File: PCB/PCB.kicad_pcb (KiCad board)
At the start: 2 copper layers, 82 x 60 mm, 118 parts, among them J1 Conn_01x02_Pin, J3 Conn_02x16_Odd_Even, J4 USB_C_Receptacle_PowerOnly_6P, SW1 SW_Nidec_CAS-120A1, U1 DRV8833PWPR, U10 TPS63020, U11 TPS63020, U12 TS5A3159ADBVR, U13 CH224K, U2 INA219AxDCN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

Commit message: Fix PCB layout
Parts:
- J1: footprint Connector_JST:JST_JWPF_B02B-JWPF-SK-R_1x02_P2.00mm_Vertical -> Connector_JST:JST_PH_S2B-PH-K_1x02_P2.00mm_Horizontal
- moved U10 233.6 mm to (176.1, 15.4), turned to 180 degrees
- moved R31 172.2 mm to (45.6, 102.0), turned to 90 degrees
- moved TP33 167.5 mm to (47.8, 93.0), turned to 90 degrees
- moved D5 166.7 mm to (55.0, 102.0)
- moved R10 164.0 mm to (52.8, 97.5)
- moved D2 163.2 mm to (57.1, 121.1), turned to -90 degrees
- moved R32 160.3 mm to (56.6, 112.0)
- moved R27 159.5 mm to (40.5, 113.1), turned to -90 degrees
- moved R24 156.3 mm to (43.5, 112.9), turned to -90 degrees
- moved C4 153.8 mm to (33.0, 112.6), turned to -90 degrees
- moved C5 150.3 mm to (36.7, 108.8)
- moved TP24 150.0 mm to (61.6, 101.5)
- moved R20 144.3 mm to (53.0, 104.5), turned to 180 degrees
- moved U3 143.2 mm to (63.6, 98.5)
- moved R19 141.4 mm to (54.1, 121.1), turned to 90 degrees
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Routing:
- net GND: track 459.7 -> 0.00 mm, vias 4 -> 0
- net Load_Supply: track 188.3 -> 0.00 mm, vias 7 -> 0
- net /5V_Out: track 158.0 -> 0.00 mm, vias 5 -> 0
- net High_Voltage_(9V): track 147.1 -> 0.00 mm, vias 7 -> 0
- net /3V3_Out: track 146.9 -> 0.00 mm, vias 5 -> 0
- net EXT_LOAD2_OUT: track 140.0 -> 0.00 mm, vias 2 -> 0
- net Net-(U10-PG): track 131.8 -> 0.00 mm, vias 2 -> 0
- net EXT_LOAD1_OUT: track 131.3 -> 0.00 mm, vias 5 -> 0
- net Net-(JP19-B): track 127.4 -> 0.00 mm, vias 7 -> 0
- net Battery: track 122.5 -> 0.00 mm, vias 4 -> 0
- net MOTOR4_A_OUT: track 111.8 -> 0.00 mm, vias 8 -> 0
- net Net-(JP18-A): track 108.3 -> 0.00 mm, vias 4 -> 0
- net Net-(JP17-B): track 104.0 -> 0.00 mm, vias 5 -> 0
- net Net-(U13-VBUS): track 102.4 -> 0.00 mm, vias 4 -> 0
- net /VBUS: track 101.3 -> 0.00 mm, vias 2 -> 0
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
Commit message: Dummy Commit
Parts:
- added REF**: MountingHole_2.1mm, MountingHole:MountingHole_2.1mm, F.Cu at (53.5, 128.5)
- moved JP16 51.2 mm to (139.2, 135.0)
- moved C2 51.2 mm to (153.0, 139.0)
- moved C3 51.2 mm to (153.0, 141.0)
- moved D1 51.2 mm to (148.4, 145.0)
- moved JP12 51.2 mm to (139.0, 139.0)
- moved JP20 51.2 mm to (138.7, 142.5)
- moved JP25 51.2 mm to (138.7, 146.5)
- moved R14 51.2 mm to (144.1, 145.0)
- moved R23 51.2 mm to (135.0, 137.1)
- moved TP6 51.2 mm to (152.0, 137.0)
- moved TP7 51.2 mm to (154.5, 137.0)
- moved TP8 51.2 mm to (153.0, 148.0)
- moved TP9 51.2 mm to (149.0, 148.5)
- moved U1 51.2 mm to (146.0, 140.0)
- moved C16 51.2 mm to (152.1, 145.0)
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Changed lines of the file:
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@@
 	(footprint "Resistor_SMD:R_0603_1608Metric_Pad0.98x0.95mm_HandSolder"
 		(layer "F.Cu")
-		(at 99.6876 119.4751 180)
+		(at 144.0875 145 180)
 		(descr "Resistor SMD 0603 (1608 Metric), square (rectangular) end terminal, IPC_7351 nominal with elongated pad for handsoldering. (Body size source: IPC-SM-782 page 72, https://www.pcb-3d.com/wordpress/wp-content/uploads/ipc-sm-782a_amendment_1_and_2.pdf), generated with kicad-footprint-generator")
 		(tags "resistor handsolder")
@@
 	(footprint "Jumper:SolderJumper-2_P1.3mm_Open_Pad1.0x1.5mm"
 		(layer "F.Cu")
-		(at 94.35 121 180)
+		(at 138.7499 146.5249 180)
 		(descr "SMD Solder Jumper, 1x1.5mm Pads, 0.3mm gap, open")
 		(tags "solder jumper open")
@@
 	(footprint "TestPoint:TestPoint_Pad_D1.0mm"
 		(layer "F.Cu")
-		(at 107.6001 111.4751)
+		(at 152 137)
 		(descr "SMD pad as test Point, diameter 1.0mm")
 		(tags "test point SMD pad")
@@
 	(footprint "TestPoint:TestPoint_Pad_D1.0mm"
 		(layer "F.Cu")
-		(at 104.6001 122.9751)
+		(at 149 148.5)
 		(descr "SMD pad as test Point, diameter 1.0mm")
 		(tags "test point SMD pad")
@@
 	(footprint "Jumper:SolderJumper-2_P1.3mm_Open_Pad1.0x1.5mm"
 		(layer "F.Cu")
-		(at 94.8 109.5 180)
+		(at 139.1999 135.0249 180)
 		(descr "SMD Solder Jumper, 1x1.5mm Pads, 0.3mm gap, open")
 		(tags "solder jumper open")
@@
 	(footprint "Capacitor_SMD:C_0603_1608Metric_Pad1.08x0.95mm_HandSolder"
 		(layer "F.Cu")
-		(at 107.7376 119.4751 180)
+		(at 152.1375 145 180)
 		(descr "Capacitor SMD 0603 (1608 Metric), square (rectangular) end terminal, IPC_7351 nominal with elongated pad for handsoldering. (Body size source: IPC-SM-782 page 76, https://www.pcb-3d.com/wordpress/wp-content/uploads/ipc-sm-782a_amendment_1_and_2.pdf), generated with kicad-footprint-generator")
 		(tags "capacitor handsolder")
@@
 	(footprint "Resistor_SMD:R_0603_1608Metric_Pad0.98x0.95mm_HandSolder"
 		(layer "F.Cu")
-		(at 90.7 118.9125 90)
+		(at 135.0999 144.4374 90)
 		(descr "Resistor SMD 0603 (1608 Metric), square (rectangular) end terminal, IPC_7351 nominal with elongated pad for handsoldering. (Body size source: IPC-SM-782 page 72, https://www.pcb-3d.com/wordpress/wp-content/uploads/ipc-sm-782a_amendment_1_and_2.pdf), generated with kicad-footprint-generator")
 		(tags "resistor handsolder")
@@
 	(footprint "Capacitor_SMD:C_0603_1608Metric_Pad1.08x0.95mm_HandSolder"
 		(layer "F.Cu")
-		(at 108.6001 113.4751 180)
+		(at 153 139 180)
 		(descr "Capacitor SMD 0603 (1608 Metric), square (rectangular) end terminal, IPC_7351 nominal with elongated pad for handsoldering. (Body size source: IPC-SM-782 page 76, https://www.pcb-3d.com/wordpress/wp-content/uploads/ipc-sm-782a_amendment_1_and_2.pdf), generated with kicad-footprint-generator")
 		(tags "capacitor handsolder")
@@
 	(footprint "LED_SMD:LED_0603_1608Metric_Pad1.05x0.95mm_HandSolder"
 		(layer "F.Cu")
-		(at 103.9751 119.4751 180)
+		(at 148.375 145 180)
 		(descr "LED SMD 0603 (1608 Metric), square (rectangular) end terminal, IPC_7351 nominal, (Body size source: http://www.tortai-tech.com/upload/download/2011102023233369053.pdf), generated with kicad-footprint-generator")
 		(tags "LED handsolder")
@@
 	(footprint "Mix:IC_DRV8833PWPR"
 		(layer "F.Cu")
-		(at 101.6001 114.4751)
+		(at 146 140)
 		(property "Reference" "U1"
 			(at -0.375038 -3.432776 0)
@@
 			(polygon
 				(pts
-					(xy 100.37 115.63) (xy 102.8302 115.63) (xy 102.8302 113.3202) (xy 100.37 113.3202)
+					(xy 144.7699 141.1549) (xy 147.2301 141.1549) (xy 147.2301 138.8451) (xy 144.7699 138.8451)
 				)
 			)
@@
 			(polygon
 				(pts
-					(xy 100.37 115.63) (xy 102.8302 115.63) (xy 102.8302 113.3202) (xy 100.37 113.3202)
+					(xy 144.7699 141.1549) (xy 147.2301 141.1549) (xy 147.2301 138.8451) (xy 144.7699 138.8451)
 				)
 			)
@@
 		)
 	)
+	(footprint "MountingHole:MountingHole_2.1mm"
+		(layer "F.Cu")
+		(at 53.5 128.5)
+		(descr "Mounting Hole 2.1mm, no annular")
+		(tags "mounting hole 2.1mm no annular")
+		(property "Reference" "REF**"
+			(at 0 -3.2 0)
+			(layer "F.SilkS")
+			(effects
+				(font
+					(size 1 1)
+					(thickness 0.15)
+				)
+			)
+		)
+		(property "Value" "MountingHole_2.1mm"
+			(at 0 3.2 0)
+			(layer "F.Fab")
+			(effects
+				(font
+					(size 1 1)
+					(thickness 0.15)
+				)
+			)
+		)
+		(property "Datasheet" ""
+			(at 0 0 0)
+			(unlocked yes)
+			(layer "F.Fab")
+			(hide yes)
+			(effects
+				(font
+					(size 1.27 1.27)
+					(thickness 0.15)
+				)
+			)
+		)
+		(property "Description" ""
+			(at 0 0 0)
+			(unlocked yes)
+			(layer "F.Fab")
+			(hide yes)
+			(effects
+				(font
+					(size 1.27 1.27)
+					(thickness 0.15)
+				)
+			)
+		)
+		(attr exclude_from_pos_files exclude_from_bom)
+		(fp_circle
+			(center 0 0)
+			(end 2.1 0)
+			(stroke
+				(width 0.15)
+				(type solid)
+			)
+			(fill no)
+			(layer "Cmts.User")
+		)
+		(fp_circle
+			(center 0 0)
+			(end 2.35 0)
+			(stroke
+				(width 0.05)
+				(type solid)
+			)
+			(fill no)
+			(layer "F.CrtYd")
+		)
+		(fp_text user "${REFERENCE}"
+			(at 0 0 0)
+			(layer "F.Fab")
+			(effects
+				(font
+					(size 1 1)
+					(thickness 0.15)
+				)
+			)
+		)
+		(pad "" np_thru_hole circle
+			(at 0 0)
+			(size 2.1 2.1)
+			(drill 2.1)
+			(layers "*.Cu" "*.Mask")
+		)
+		(embedded_fonts no)
+	)
 	(footprint "Jumper:SolderJumper-3_P1.3mm_Open_Pad1.0x1.5mm"
 		(layer "F.Cu")
@@
 	(footprint "Capacitor_SMD:C_0603_1608Metric_Pad1.08x0.95mm_HandSolder"
 		(layer "F.Cu")
-		(at 108.6001 115.4751)
+		(at 153 141)
 		(descr "Capacitor SMD 0603 (1608 Metric), square (rectangular) end terminal, IPC_7351 nominal with elongated pad for handsoldering. (Body size source: IPC-SM-782 page 76, https://www.pcb-3d.com/wordpress/wp-content/uploads/ipc-sm-782a_amendment_1_and_2.pdf), generated with kicad-footprint-generator")
 		(tags "capacitor handsolder")
@@
 	(footprint "Jumper:SolderJumper-2_P1.3mm_Open_Pad1.0x1.5mm"
 		(layer "F.Cu")
-		(at 94.35 117 180)
+		(at 138.7499 142.5249 180)
 		(descr "SMD Solder Jumper, 1x1.5mm Pads, 0.3mm gap, open")
 		(tags "solder jumper open")
@@
 	(footprint "TestPoint:TestPoint_Pad_D1.0mm"
 		(layer "F.Cu")
-		(at 110.1001 111.4751)
+		(at 154.5 137)
 		(descr "SMD pad as test Point, diameter 1.0mm")
 		(tags "test point SMD pad")
@@
 	(footprint "Jumper:SolderJumper-2_P1.3mm_Open_Pad1.0x1.5mm"
 		(layer "F.Cu")
-		(at 94.65 113.5 180)
+		(at 139.0499 139.0249 180)
 		(descr "SMD Solder Jumper, 1x1.5mm Pads, 0.3mm gap, open")
 		(tags "solder jumper open")
@@
 	(footprint "Resistor_SMD:R_0603_1608Metric_Pad0.98x0.95mm_HandSolder"
 		(layer "F.Cu")
-		(at 90.65 111.5875 90)
+		(at 135.0499 137.1124 90)
 		(descr "Resistor SMD 0603 (1608 Metric), square (rectangular) end terminal, IPC_7351 nominal with elongated pad for handsoldering. (Body size source: IPC-SM-782 page 72, https://www.pcb-3d.com/wordpress/wp-content/uploads/ipc-sm-782a_amendment_1_and_2.pdf), generated with kicad-footprint-generator")
 		(tags "resistor handsolder")
@@
 	(footprint "TestPoint:TestPoint_Pad_D1.0mm"
 		(layer "F.Cu")
-		(at 108.6001 122.4751)
+		(at 153 148)
 		(descr "SMD pad as test Point, diameter 1.0mm")
 		(tags "test point SMD pad")

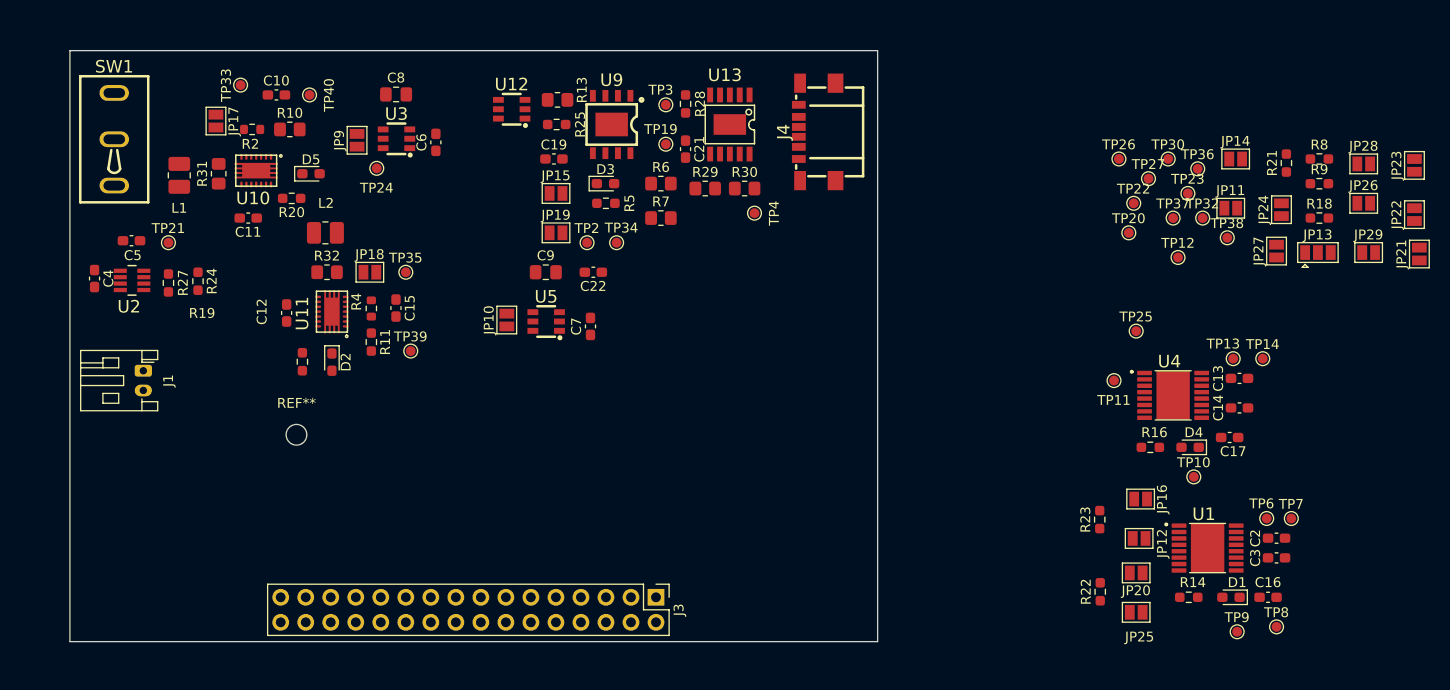
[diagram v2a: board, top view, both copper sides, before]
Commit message: Placing All components onto the silkscreen
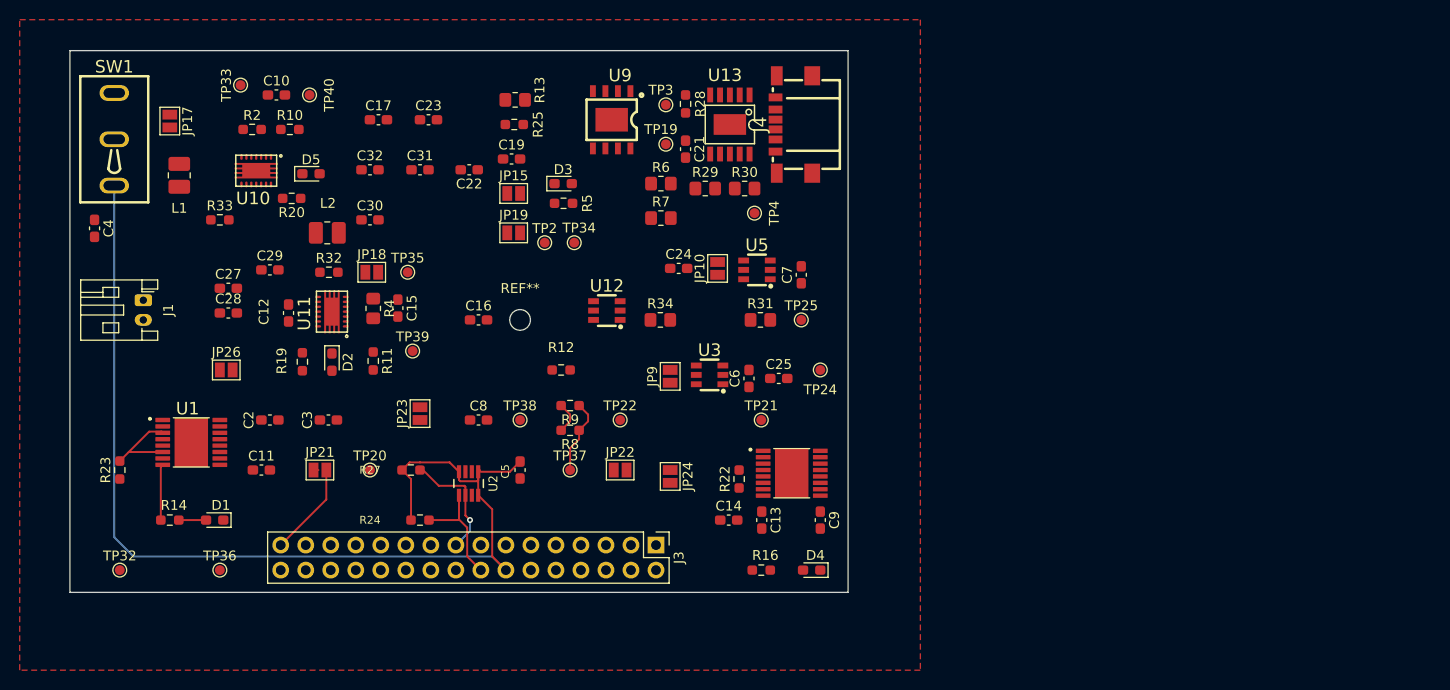
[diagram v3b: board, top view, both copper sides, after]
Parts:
- removed JP11, JP12, JP14, JP16, JP20, JP25, JP27, JP28, JP29: Jumper_2_Small_Open, Jumper:SolderJumper-2_P1.3mm_Open_Pad1.0x1.5mm
- removed JP13: Jumper_3_Open, Jumper:SolderJumper-3_P1.3mm_Open_Pad1.0x1.5mm
- removed R18, R21: 0.22, Resistor_SMD:R_0603_1608Metric_Pad0.98x0.95mm_HandSolder
- removed TP10, TP11, TP12, TP13, TP14, TP23, TP26, TP27, TP30, TP6, TP7, TP8, TP9: TestPoint, TestPoint:TestPoint_Pad_D1.0mm
- added C23: 10u, Capacitor_SMD:C_0603_1608Metric_Pad1.08x0.95mm_HandSolder, F.Cu at (66.9, 96.5)
- added C24: 10u, Capacitor_SMD:C_0603_1608Metric_Pad1.08x0.95mm_HandSolder, F.Cu at (92.3, 111.6)
- added C25: 10u, Capacitor_SMD:C_0603_1608Metric_Pad1.08x0.95mm_HandSolder, F.Cu at (102.5, 122.8)
- added C27: 22u, Capacitor_SMD:C_0603_1608Metric_Pad1.08x0.95mm_HandSolder, F.Cu at (46.6, 113.6)
- added C28: 22u, Capacitor_SMD:C_0603_1608Metric_Pad1.08x0.95mm_HandSolder, F.Cu at (46.6, 116.1)
- added C29: 22u, Capacitor_SMD:C_0603_1608Metric_Pad1.08x0.95mm_HandSolder, F.Cu at (50.8, 111.8)
- added C30: 22u, Capacitor_SMD:C_0603_1608Metric_Pad1.08x0.95mm_HandSolder, F.Cu at (61.0, 106.7)
- added C31: 22u, Capacitor_SMD:C_0603_1608Metric_Pad1.08x0.95mm_HandSolder, F.Cu at (66.0, 101.6)
- added C32: 22u, Capacitor_SMD:C_0603_1608Metric_Pad1.08x0.95mm_HandSolder, F.Cu at (61.0, 101.6)
- added R12: 0.22, Resistor_SMD:R_0603_1608Metric_Pad0.98x0.95mm_HandSolder, F.Cu at (80.4, 121.9)
- added R33: 510k, Resistor_SMD:R_0603_1608Metric_Pad0.98x0.95mm_HandSolder, F.Cu at (45.7, 106.7)
- added R34: 10k, Resistor_SMD:R_0805_2012Metric_Pad1.20x1.40mm_HandSolder, F.Cu at (90.4, 116.8)
- C11: value 10u -> 100n
- C13, C16, C17: value 2.2u -> 10u
- C14: value 10u -> 2.2u
- C5: value 0.1u -> 100n
- C8, C9: value 47u -> 100n; footprint Capacitor_SMD:C_0805_2012Metric_Pad1.18x1.45mm_HandSolder -> Capacitor_SMD:C_0603_1608Metric_Pad1.08x0.95mm_HandSolder
- R10: value 200 -> 56k; footprint Resistor_SMD:R_0805_2012Metric_Pad1.20x1.40mm_HandSolder -> Resistor_SMD:R_0603_1608Metric_Pad0.98x0.95mm_HandSolder
- R11: value 100 -> 82k
- R2: value 1.8k -> 510k; footprint Resistor_SMD:R_0603_1608Metric -> Resistor_SMD:R_0603_1608Metric_Pad0.98x0.95mm_HandSolder
- R32: value 10k -> 510k; footprint Resistor_SMD:R_0805_2012Metric_Pad1.20x1.40mm_HandSolder -> Resistor_SMD:R_0603_1608Metric_Pad0.98x0.95mm_HandSolder
- R4: value 560 -> 470k; footprint Resistor_SMD:R_0603_1608Metric -> Resistor_SMD:R_0805_2012Metric_Pad1.20x1.40mm_HandSolder
- moved JP26 116.7 mm to (46.4, 121.9)
- moved TP32 115.6 mm to (35.6, 142.2)
- moved JP21 113.8 mm to (55.9, 132.1), turned to 0 degrees
- moved TP36 107.3 mm to (45.7, 142.2)
- moved JP23 104.1 mm to (66.0, 126.3)
- moved R14 103.7 mm to (40.6, 137.2)
- moved U1 103.7 mm to (42.8, 129.3)
- moved D1 103.5 mm to (45.2, 137.2)
- moved C2 102.9 mm to (50.8, 127.0)
- moved R23 99.6 mm to (35.6, 132.1)
- moved C3 97.3 mm to (56.7, 127.0)
- moved C17 92.2 mm to (61.8, 96.5), turned to 0 degrees
- moved C16 85.0 mm to (72.0, 116.8), turned to 0 degrees
- moved JP22 84.7 mm to (86.4, 132.1), turned to 0 degrees
- moved R8 80.9 mm to (81.3, 128.0), turned to 180 degrees
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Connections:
- net /M4AB2 renamed /M4BO2
- C11 pad 1: Load_Supply -> 5V Out
- C11 pad 2: GND -> Net-(U1-VCP)
- C13 pad 1: GND -> 5V Out
- C13 pad 2: Net-(U4-VINT) -> GND
- C14 pad 1: Load_Supply -> GND
- C14 pad 2: GND -> Net-(U4-VINT)
- C16 pad 2: Net-(U1-VCP) -> GND
- C17 pad 1: Net-(U4-VINT) -> Load_Supply
- C17 pad 2: Net-(U4-VCP) -> GND
- C3 pad 1: Load_Supply -> 5V Out
- C6 pad 1: /5V_Out -> 5V Out
- C7 pad 1: /5V_Out -> 5V Out
- C8 pad 1: EXT_LOAD1_OUT -> Battery
- C8 pad 2: GND -> Load_Supply
- C9 pad 1: EXT_LOAD2_OUT -> 5V Out
- C9 pad 2: GND -> Net-(U4-VCP)
- J3 pad 18: /3V3_Out -> 3V3 Out
- J3 pad 20: /5V_Out -> 5V Out
- JP17 pad 1: /5V_Out -> 5V Out
- JP26 pad 1: /AISEN3 -> 3V3 Out
- R2 pad 1: /5V_Out -> 5V Out
- R22 pad 2: Net-(JP20-B) -> /SEN2
- R23 pad 2: Net-(JP16-B) -> /SEN1
- R30 pad 2: /VBUS -> High_Voltage_(9V)
- R31 pad 1: Net-(U10-PG) -> Net-(U5-QOD)
- R31 pad 2: Net-(JP17-B) -> Net-(JP10-A)
- R32 pad 2: Net-(JP18-A) -> Net-(JP26-B)
- R4 pad 1: /5V_Out -> 3V3 Out
- R8 pad 2: Net-(JP13-A) -> Load_Supply
- R9 pad 2: Net-(JP13-B) -> Load_Supply
- TP35 pad 1: /3V3_Out -> Net-(JP26-B)
- TP4 pad 1: /VBUS -> High_Voltage_(9V)
- U1 pad 1: /5V_Out -> Battery
- U1 pad 12: Load_Supply -> 5V Out
- U1 pad 3: /AISEN1 -> /SEN1
- U1 pad 5: /M2AO2 -> /M2BO2
- U1 pad 6: /BISEN1 -> /SEN1
- U1 pad 7: /M2AO1 -> MOTOR2_A_OUT
- U10 pad 5: /5V_VOUT2 -> Net-(JP17-B)
- U11 pad 4: Net-(JP18-A) -> Net-(JP26-B)
- U11 pad 5: /3V3_VOUT2 -> Net-(JP26-B)
- U3 pad 1: /5V_Out -> 5V Out
- U3 pad 4: /5V_Out -> 5V Out
- U3 pad 5: EXT_LOAD1_OUT -> Net-(U3-QOD)
- U4 pad 1: /5V_Out -> Battery
- U4 pad 12: Load_Supply -> 5V Out
- U4 pad 3: /AISEN2 -> /SEN2
- U4 pad 6: /BISEN2 -> /SEN2
- U5 pad 1: /5V_Out -> 5V Out
- U5 pad 4: /5V_Out -> 5V Out
- U5 pad 5: EXT_LOAD2_OUT -> Net-(U5-QOD)
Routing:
- net Battery: track 0.00 -> 116.3 mm
- net I2C1_SDA: track 0.00 -> 12.0 mm, vias 0 -> 1
- net I2C1_SCL: track 0.00 -> 11.6 mm
- net MOTOR1_B_OUT: track 0.00 -> 9.54 mm
- net /SEN1: track 0.00 -> 9.09 mm
- net Net-(U1-~{FAULT}): track 0.00 -> 5.69 mm
- net Load_Supply: track 0.00 -> 3.27 mm
- net Net-(D1-A): track 0.00 -> 2.77 mm
- added copper zone on F.Cu, net GND
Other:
- board size 82 x 60 mm -> 79 x 55 mm

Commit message: Routing
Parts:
- removed the REF** at (76.2, 116.8)
- removed U12: TS5A3159ADBVR, Mix:SOT-23-6_L2.9-W1.6-P0.95-LS2.8-BR
- added JP20: Jumper_2_Small_Open, Jumper:SolderJumper-2_P1.3mm_Open_Pad1.0x1.5mm, F.Cu at (61.2, 122.7)
- added JP25: Jumper_2_Small_Open, Jumper:SolderJumper-2_P1.3mm_Open_Pad1.0x1.5mm, F.Cu at (56.9, 136.7)
- added REF**: MountingHole_3.2mm_M3, MountingHole:MountingHole_3.2mm_M3, F.Cu at (73.5, 133.2)
- added U6: TS5A3159ADBVR, Mix:SOT-23-6_L2.9-W1.6-P0.95-LS2.8-BR, F.Cu at (57.0, 122.7)
- moved U10 293.7 mm to (-31.2, 223.5), turned to 0 degrees
- moved U11 282.4 mm to (3.40, -2.54), turned to -90 degrees
- moved SW1 84.2 mm to (108.0, 140.5), turned to 180 degrees
- moved C4 80.6 mm to (110.0, 131.5), turned to 90 degrees
- moved J4 79.1 mm to (39.0, 142.0), turned to -90 degrees
- moved JP17 76.8 mm to (102.4, 142.3), turned to 90 degrees
- moved TP32 74.5 mm to (101.5, 107.7), turned to 180 degrees
- moved TP33 71.1 mm to (95.2, 146.0), turned to -90 degrees
- moved L1 69.1 mm to (101.4, 136.8), turned to 90 degrees
- moved U13 68.8 mm to (45.5, 142.0), turned to 0 degrees
- moved C7 68.1 mm to (38.2, 126.7), turned to -90 degrees
- moved R23 68.0 mm to (100.5, 112.1), turned to -90 degrees
- moved J1 67.7 mm to (105.0, 124.2), turned to 90 degrees
- moved TP25 66.7 mm to (38.2, 122.2), turned to 180 degrees
- moved R14 65.6 mm to (98.1, 105.7), turned to 0 degrees
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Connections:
- C21 pad 1: /3V3_Out -> Net-(JP25-A)
- R13 pad 1: Net-(U9-PROG) -> GND
- R25 pad 1: Net-(U9-PROG) -> GND
- R28 pad 2: /3V3_Out -> Net-(JP25-A)
- U13 pad 1: /3V3_Out -> Net-(JP25-A)
- U9 pad 2: Net-(U9-PROG) -> Net-(U6-COM)
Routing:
- net Battery: track 116.3 -> 0.00 mm
- net I2C1_SDA: track 12.0 -> 0.00 mm, vias 1 -> 0
- net I2C1_SCL: track 11.6 -> 0.00 mm
- net MOTOR1_B_OUT: track 9.54 -> 0.00 mm
- net /SEN1: track 9.09 -> 0.00 mm
- net Net-(U1-~{FAULT}): track 5.69 -> 0.00 mm
- net Load_Supply: track 3.27 -> 0.00 mm
- net Net-(D1-A): track 2.77 -> 0.00 mm
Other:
- board size 79 x 55 mm -> 79.5 x 58.5 mm
